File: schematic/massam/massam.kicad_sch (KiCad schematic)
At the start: 15 parts, among them J1 Conn_02x40_Row_Letter_First, U1 R6502, U2 SST39SF512, U3 UT62256PC-70LL, U4 GAL20L8, X1 1.8Mhz

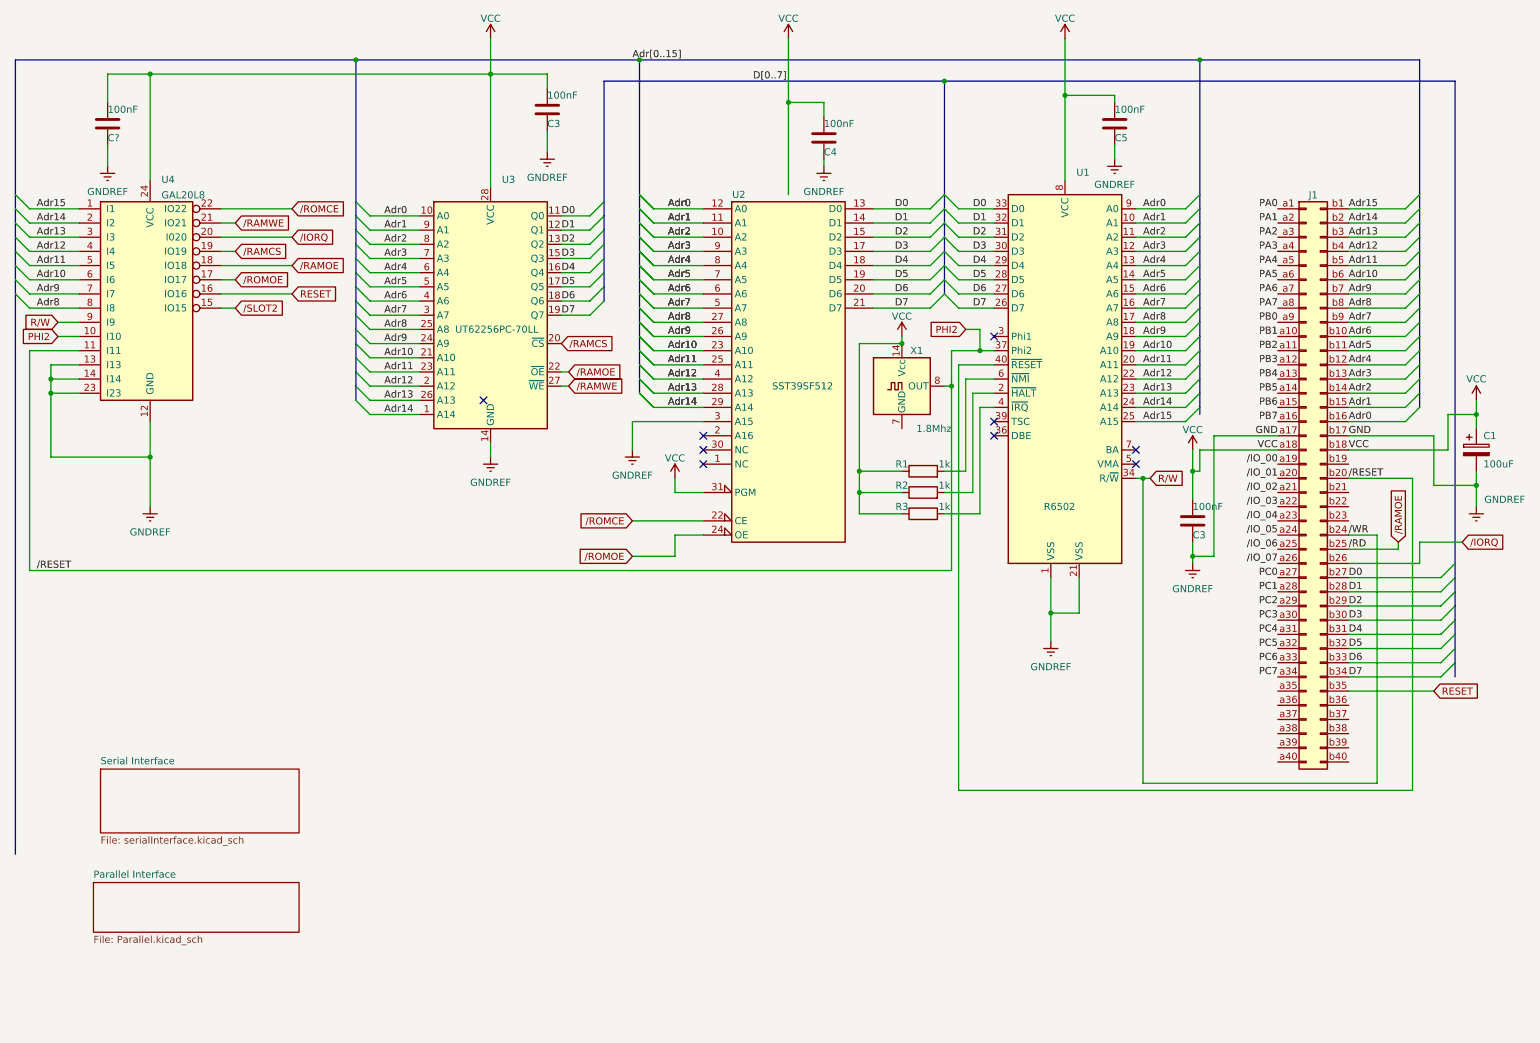
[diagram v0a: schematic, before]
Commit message: Added schematic for W65C02
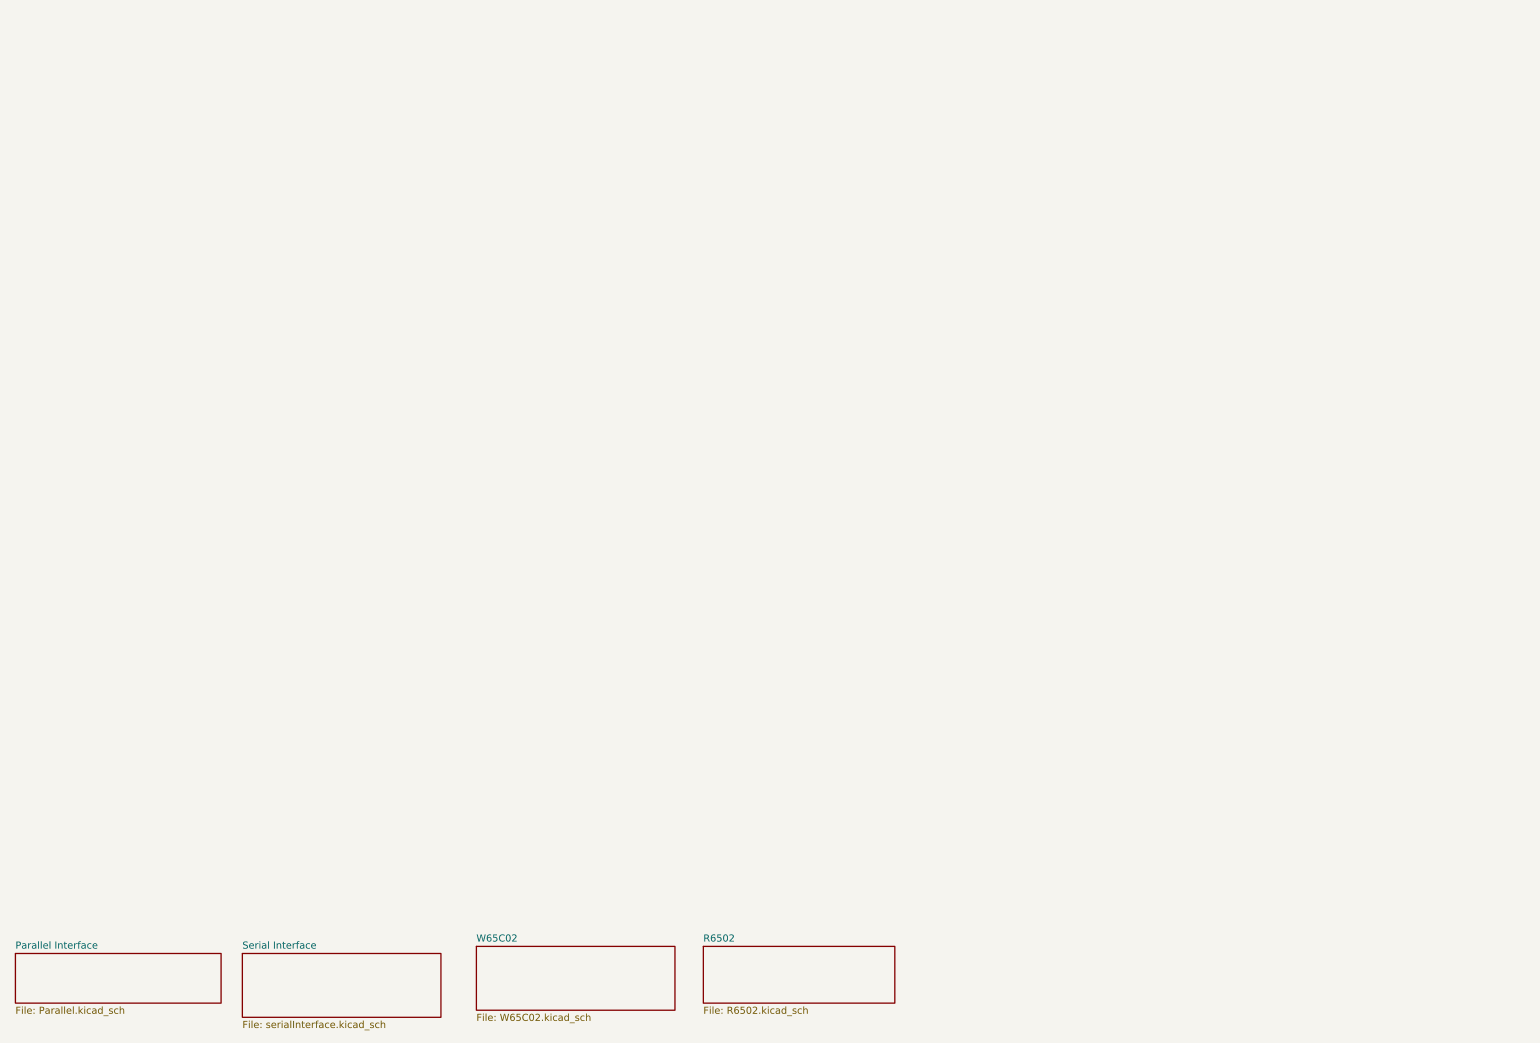
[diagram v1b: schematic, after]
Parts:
- removed C1: 100uF, symbol Device:C_Polarized
- removed C3 (x2), C4, C5, C?: 100nF, symbol Device:C
- removed J1: Conn_02x40_Row_Letter_First, symbol Connector_Generic:Conn_02x40_Row_Letter_First
- removed R1, R2, R3: 1k, symbol Device:R
- removed U1: R6502, Package_DIP:DIP-40_W15.24mm, symbol CPU_NXP_6800:MC6800
- removed U2: SST39SF512, symbol Memory_Flash:SST39SF010
- removed U3: UT62256PC-70LL, Package_DIP:DIP-28_W15.24mm, symbol Memory_RAM:HM62256BLP
- removed U4: GAL20L8, symbol Logic_Programmable:PAL20L8
- removed X1: 1.8Mhz, Oscillator:Oscillator_DIP-14, symbol Oscillator:ACO-xxxMHz
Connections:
- no-connect marks 9 -> 0
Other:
- added sheet R6502 (R6502.kicad_sch)
- added sheet W65C02 (W65C02.kicad_sch)
- title: SPARTAN -> HMC56
